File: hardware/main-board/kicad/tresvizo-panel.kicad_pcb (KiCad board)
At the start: 4 copper layers, 82.8 x 78 mm, 141 parts, among them J101 PANEL_USB, J102 BATTERY, J301 GNSS, J401 TF-015, J402 BOTON, J403 OLED, J404 NTC, J405 IMU, J406 LEDS, J501 USB_C, J502 PANEL_USB, Q101 AO3400A, Q102 AO3401A, Q103 AO3400A, Q401 AO3401A, Q402 AO3400A, SW201 RESET, SW202 BOOT, U101 USBLC6-2SC6, U102 BQ25798RQMR, U103 MAX17048G+T10, U105 TPS62903RPJR, U201 ESP32-S3-MINI-1-N4R2, U301 TPS63070RNMR, U302 USBLC6-2SC6, U303 USBLC6-2SC6, U501 USBLC6-2SC6

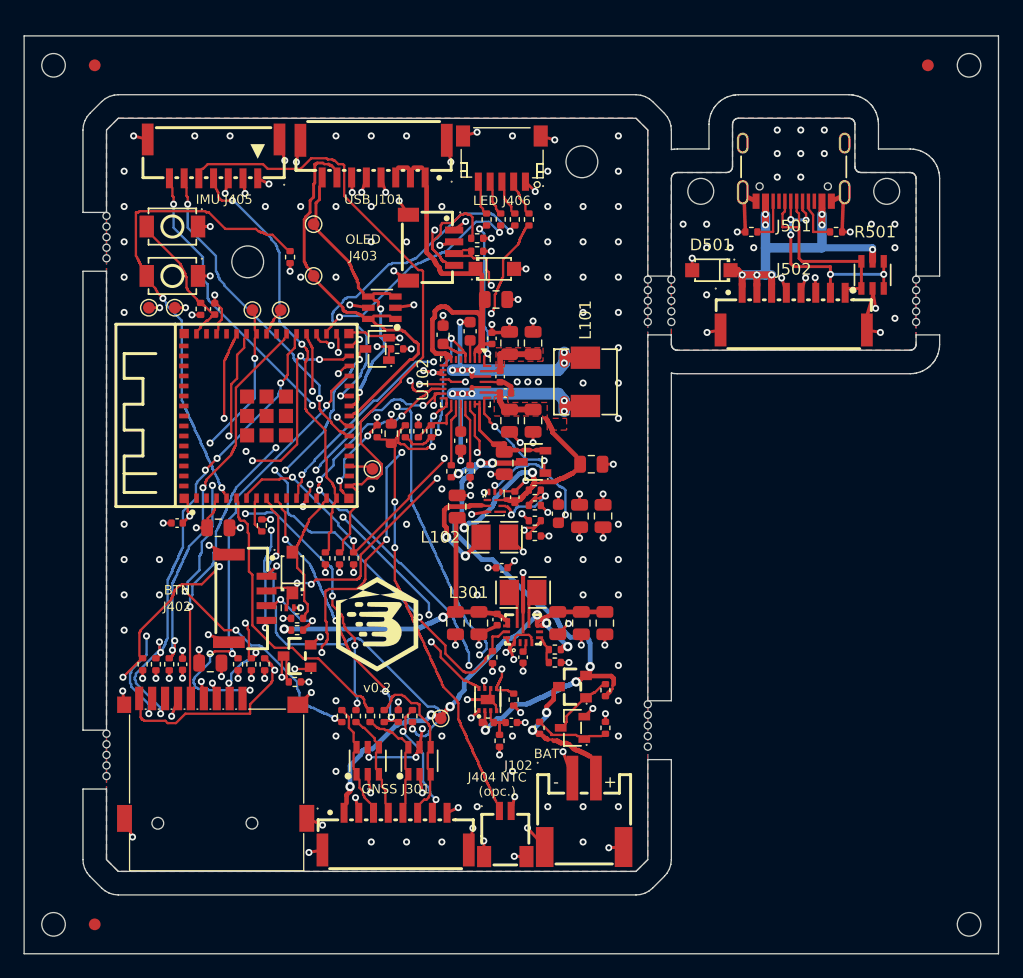
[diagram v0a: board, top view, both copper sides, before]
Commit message: Placa principal v0.2: J404 montado con puente JP101, USB-C de la panel-usb más volado, correcciones de la auditoría y logotipo
- J404 (NTC) se monta de fábrica y la NTC queda opcional. Sin ella, R106 (10 kΩ) va a GND por
  JP101, un puente de soldadura cerrado de fábrica, y el cargador ve 25 °C. Para usar la NTC se
  corta JP101 («cortar JP101» en la serigrafía, sobre el puente). R115 baja junto a R113 para
  dejar sitio a esa línea.
- panel-usb: el canto de la lengüeta retrocede 0.8 mm (v = 0.89) y el USB-C sobresale 1.29 mm; su
  cara sigue a ras de la tapa. El cobre queda a 0.41 mm del canto. En el panel la fresa frente al
  USB-C se ensancha a 3 mm (opción cuts de panelize.py) para dejar 1.71 mm hasta el marco; el
  panel pasa a 82.8 x 79 mm.
- Auditoría: VBUS de J101 al cargador con pistas de 0.8 y 1.0 mm, etiquetas de la batería y del
  NTC separadas, planos internos con 0.12 mm de margen y, en el README, medir el pin 1 de la
  carrier antes de enchufar el arnés y la ranura propuesta en la base bajo J102.
- Logotipo: las piezas con huecos se parten en tiras, porque KiCad deformaba al guardar los
  contornos fracturados (el distintivo de la cara de componentes salía mal).
- ERC 0; DRC con 0 errores, 0 avisos, 0 sin conectar y 0 diferencias de paridad en las dos placas
  y el panel. Comprobación en FreeCAD contra V2.2 sin choques nuevos. Costo estimado de montaje y
  piezas: 213.60 USD por 5 juegos en un panel (J404 suma 2.22 USD), sin el PCB desnudo.
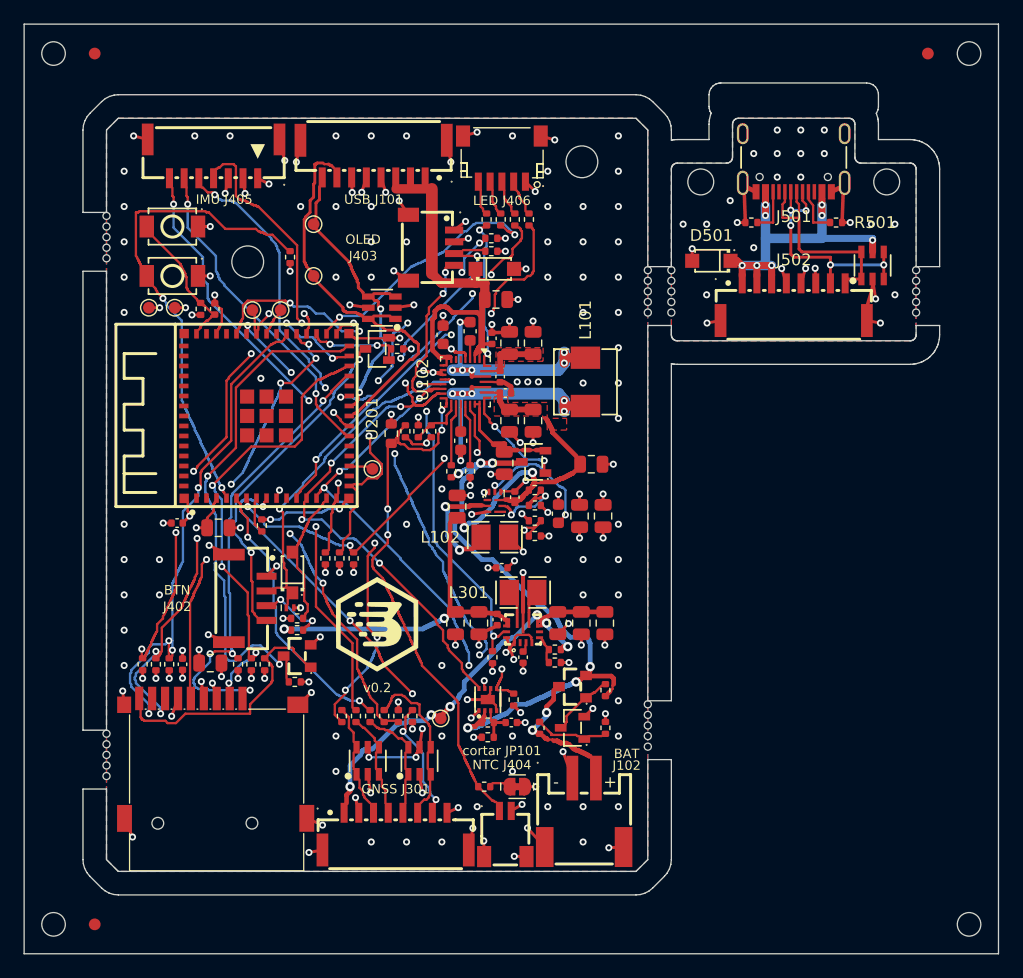
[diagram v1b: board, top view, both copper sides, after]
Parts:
- added JP101: NTC_CORTAR, tresvizo_lcsc:SolderJumper-2_P1.3mm_Bridged_RoundedPad1.0x1.5mm, F.Cu at (141.9, 163.8)
- moved R106 31.5 mm to (139.1, 163.8), turned to 0 degrees
- moved R204 1.20 mm to (139.7, 118.3)
- moved R205 1.20 mm to (139.7, 117.2)
- moved R115 1.04 mm to (139.4, 159.6), turned to 0 degrees
- moved FID1 1.00 mm to (106.0, 101.5)
- moved FID2 1.00 mm to (176.8, 101.5)
- moved TH1 1.00 mm to (102.5, 101.5)
- moved TH2 1.00 mm to (180.3, 101.5)
- moved U501 0.80 mm to (172.1, 119.5)
- moved D501 0.80 mm to (158.4, 119.1)
- moved H501 0.80 mm to (157.5, 112.4)
- moved H502 0.80 mm to (173.3, 112.4)
- moved J501 0.80 mm to (165.4, 110.8)
- moved J502 0.80 mm to (165.4, 122.6)
- moved MB3 0.80 mm to (153.0, 119.9)
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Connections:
- R106 pad 2: GND -> /Alimentación, carga y batería/CHG_TS_FIJA
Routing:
- net IMU_SCL: track 53.8 -> 40.3 mm, vias 0 -> 3
- net I2C_SCL: track 67.7 -> 55.8 mm, vias 7 -> 9
- net LED_G: track 30.3 -> 23.5 mm, vias 2 -> 3
- net FG_ALRT_N: track 38.3 -> 45.0 mm, vias 4 -> 6
- net GNSS_RESET_MCU: track 33.7 -> 28.4 mm, vias 2 -> 4
- net SD_D3: track 33.7 -> 37.9 mm
- net I2C_SDA: track 64.5 -> 60.4 mm, vias 9 -> 7
- net SD_CLK: track 34.2 -> 37.7 mm, vias 3 -> 2
- net GNSS_PWR_EN: track 44.6 -> 47.9 mm, vias 3 -> 4
- net /Alimentación, carga y batería/VBUS: track 34.0 -> 37.3 mm
- net IMU_SDA: track 35.3 -> 38.2 mm
- net ESP_TX0: track 44.1 -> 46.9 mm, vias 6 -> 4
- net /Alimentación, carga y batería/VPACK: track 50.6 -> 53.3 mm
- net LED_B: track 19.3 -> 21.3 mm
- net BTN_N: track 30.7 -> 28.8 mm, vias 4 -> 2
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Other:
- board size 82.8 x 78 mm -> 82.8 x 79 mm
- board text added: "NTC J404"
- board text added: "cortar JP101"
- board text removed: "(opc.)"
- board text removed: "J404 NTC"

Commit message: Placa principal v0.2: techo de entrada del USB a ~1.45 A (R102 22k -> 8.2k)
Revisión del propietario: con ILIM en 10k/22k el cargador podía pedir ~2.9 A a cualquier puerto,
sin detectar cuánto da. Con 10k/8.2k desde REGN (4.6-5.0 V) el techo queda en 1.34-1.56 A, que
alcanza para cargar 1S a 1 A con el equipo encendido. La variante 2S vuelve a 22k (~2.9 A).
Solo cambia el valor de R102 (C25924): pistas y gerbers de cobre iguales; ERC 0, DRC 0 en la
placa y en el panel, paridad 0.

README: queda para v0.3 la detección por CC del USB-C y el par diferencial D+/D-, que pide
invertir los pines 7/8 de J101 y J502. En Full Speed la diferencia de largo actual (9 mm, unos
60 ps) no afecta.
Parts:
- R102: value 22k -> 8.2k

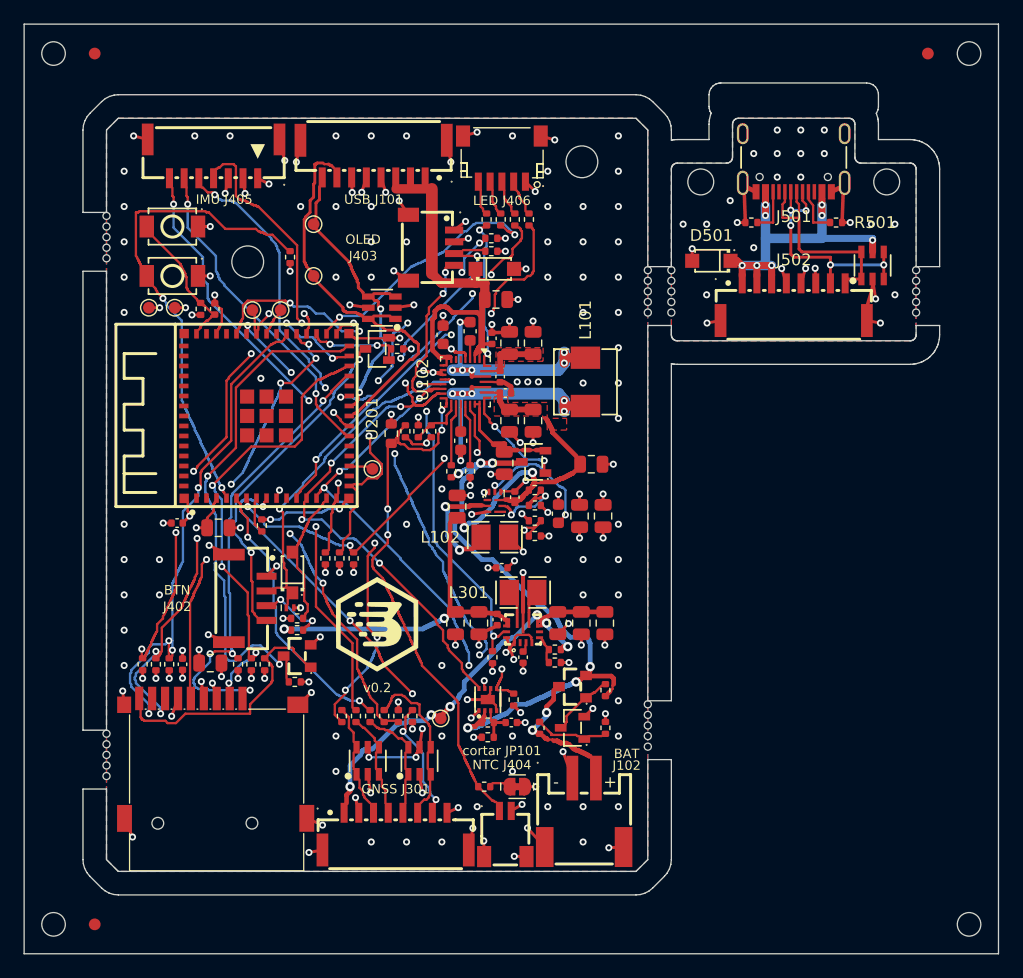
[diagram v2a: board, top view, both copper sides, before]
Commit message: Placa principal v0.2: ESP32-S3-WROOM-1-N16R2 en lugar del MINI-1 y sin LEDs del panel
- U201 = ESP32-S3-WROOM-1-N16R2 (C2913205): 16 MB de flash y 2 MB de PSRAM quad. Huella y
  modelos de LCSC; el .step se corrió 3.65 mm para que coincida con su .wrl y la huella.
- GPIO nuevos para rutear el módulo en la misma placa: microSD CLK 6, CMD 7, D0 5, D1 4, D2 16,
  D3 15 y detección 17; UART del GNSS TX 8 / RX 9; PPS 10, EVENT 11, RESET 12; I2C 13/14;
  IMU 41/42 con INT1 2 e INT3 1; botón 18; puntos de prueba en 35, 36 y 37. README y pinout
  con el mapa para el firmware.
- Fuera J406, sus resistencias y la del STAT del cargador: la carcasa V2.3 no lleva LEDs.
- Misma placa de 46 x 64 mm. H1 pasa a (12.0, 9.6) y el corte del riel +X frente a la antena a
  v 15.1-34.0; antena sin cobre en u 0-6.7, v 15.7-33.7.
- R108 sale de debajo de los pines de la microSD (el ruteador se ciclaba entre SD_D3 y
  CHG_INT_N) y el divisor de TS va bajo L102.
- BUCK_SW y el PGND de U105 prerruteados: la vía que el ruteador ponía junto a L102 hacía caer
  el relleno de zonas de KiCad 10 (-11, también en kicad-cli). route_rest guarda las pistas que
  arranca mientras dura el ruteo.
- DRC 0, sin conexiones pendientes y con paridad en la placa y en el panel; ERC 0. Costo
  estimado 206.86 USD por 5 juegos (montaje + piezas, sin PCB).
- Carcasa V2.3: H1 en z 77.9, riel +X cortado en z 53.7-72.4, placa superior recortada frente
  a la antena y SMA de la carrier con las medidas de la foto. Placa nueva contra la carcasa:
  0 mm3 de choques.
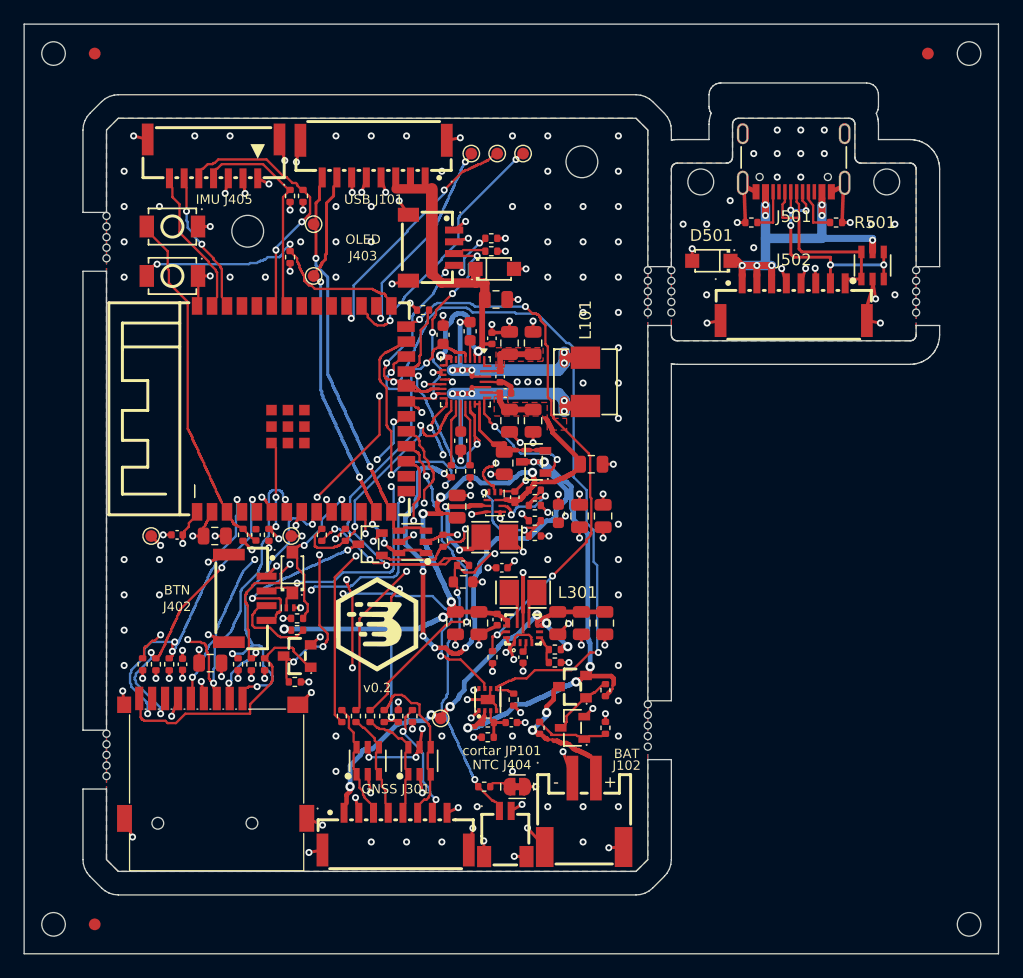
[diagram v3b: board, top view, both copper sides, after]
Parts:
- removed J406: LEDS, tresvizo_lcsc:CONN-SMD_SM05B-SRSS-TB-LF-SN
- removed R119: 22k, Resistor_SMD:R_0402_1005Metric
- removed R413: 100k, Resistor_SMD:R_0402_1005Metric
- removed R414, R415: 4.7k, Resistor_SMD:R_0402_1005Metric
- R109: value 1k -> 1M
- R110: value 1M -> 100k
- R111: value 100k -> 1M
- R112: value 1M -> 0
- R113: value 0 -> 10k
- R114: value 10k -> 0
- R115: value 0 -> 22k
- R116: value 22k -> 10k
- R117: value 10k -> 100k
- R118: value 100k -> 22k
- R409: value 1k -> 100
- R410: value 100 -> 100k
- R411, R412: value 100 -> 4.7k
- TP203: value IO14 -> IO35
- TP204: value IO42 -> IO36
- TP205: value TXD0 -> IO37
- U201: value ESP32-S3-MINI-1-N4R2 -> ESP32-S3-WROOM-1-N16R2; footprint tresvizo_lcsc:BULETM-SMD_ESP32-S3-MINI-1-N8 -> tresvizo_lcsc:WIRELM-SMD_ESP32-S3-WROOM-1
- moved R109 41.3 mm to (149.4, 155.6)
- moved R409 40.1 mm to (123.2, 150.5), turned to 0 degrees
- moved R412 36.9 mm to (123.7, 113.6), turned to 90 degrees
- moved TP203 28.1 mm to (138.0, 110.0)
- moved R410 28.0 mm to (135.6, 142.9)
- moved TP205 24.7 mm to (140.2, 110.0)
- moved TP204 24.5 mm to (142.4, 110.0)
- moved R108 21.9 mm to (133.9, 123.3), turned to 0 degrees
- moved TP202 21.8 mm to (122.7, 142.5)
- moved R115 21.4 mm to (143.4, 138.6)
- moved U101 20.1 mm to (133.0, 143.0)
- moved R201 19.5 mm to (118.6, 142.4)
- moved C203 19.5 mm to (119.7, 142.4)
- moved TP201 19.4 mm to (110.8, 142.5)
- moved R411 18.0 mm to (122.6, 113.6)
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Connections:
- R109 pad 1: /Alimentación, carga y batería/CHG_STAT -> /Alimentación, carga y batería/VPACK
- R109 pad 2: CHG_LED_K -> /Alimentación, carga y batería/BATREV_G
- R110 pad 1: /Alimentación, carga y batería/VPACK -> /Alimentación, carga y batería/VBATT_IN
- R110 pad 2: /Alimentación, carga y batería/BATREV_G -> /Alimentación, carga y batería/BATREV_SENSE
- R111 pad 1: /Alimentación, carga y batería/VBATT_IN -> /Alimentación, carga y batería/BATREV_SENSE
- R111 pad 2: /Alimentación, carga y batería/BATREV_SENSE -> GND
- R112 pad 1: /Alimentación, carga y batería/BATREV_SENSE -> /Alimentación, carga y batería/VPACK
- R112 pad 2: GND -> /Alimentación, carga y batería/FG_VDD
- R113 pad 1: /Alimentación, carga y batería/VPACK -> +3V3
- R113 pad 2: /Alimentación, carga y batería/FG_VDD -> FG_ALRT_N
- R114 pad 2: FG_ALRT_N -> /Alimentación, carga y batería/FG_VDD
- R115 pad 1: +3V3 -> VSYS
- R115 pad 2: /Alimentación, carga y batería/FG_VDD -> /Alimentación, carga y batería/BUCK_EN
- R116 pad 1: VSYS -> /Alimentación, carga y batería/BUCK_EN
- R116 pad 2: /Alimentación, carga y batería/BUCK_EN -> GND
- R117 pad 1: /Alimentación, carga y batería/BUCK_EN -> +3V3
- R117 pad 2: GND -> /Alimentación, carga y batería/BUCK_FB
- R118 pad 1: +3V3 -> /Alimentación, carga y batería/BUCK_FB
- R118 pad 2: /Alimentación, carga y batería/BUCK_FB -> GND
- R304 pad 1: ESP_TX0 -> GNSS_TX_MCU
- R409 pad 1: LED_R -> VSYS
- R409 pad 2: /microSD, IMU por conector y panel/LED_R_K -> /microSD, IMU por conector y panel/BTN_LED_A
- R410 pad 1: LED_G -> BTN_LED_EN
- R410 pad 2: /microSD, IMU por conector y panel/LED_G_K -> GND
- R411 pad 1: LED_B -> +3V3
- R411 pad 2: /microSD, IMU por conector y panel/LED_B_K -> IMU_SDA
- R412 pad 1: VSYS -> +3V3
- R412 pad 2: /microSD, IMU por conector y panel/BTN_LED_A -> IMU_SCL
- TP203 pad 1: /ESP32-S3/ESP_IO14 -> /ESP32-S3/ESP_IO35
- TP204 pad 1: /ESP32-S3/ESP_IO42 -> /ESP32-S3/ESP_IO36
- TP205 pad 1: ESP_TX0 -> /ESP32-S3/ESP_IO37
- U102 pad 1: /Alimentación, carga y batería/CHG_STAT -> unconnected-(U102-STAT-Pad1)
- U201 pad 10: unconnected-(U201-IO6-Pad10) -> SD_DET
- U201 pad 11: LED_R -> BTN_SENSE_N
- U201 pad 12: I2C_SDA -> GNSS_TX_MCU
- U201 pad 13: I2C_SCL -> USB_DN
- U201 pad 14: BTN_SENSE_N -> USB_DP
- U201 pad 15: IMU_SDA -> /ESP32-S3/ESP_IO3
- U201 pad 16: IMU_SCL -> unconnected-(U201-IO46-Pad16)
- U201 pad 17: unconnected-(U201-IO13-Pad17) -> GNSS_TXD2_MCU
- U201 pad 18: /ESP32-S3/ESP_IO14 -> GNSS_PPS_MCU
- U201 pad 19: unconnected-(U201-IO15-Pad19) -> GNSS_EVENT_MCU
- U201 pad 2: GND -> +3V3
- U201 pad 20: unconnected-(U201-IO16-Pad20) -> GNSS_RESET_MCU
- U201 pad 21: IMU_INT1 -> I2C_SDA
- U201 pad 22: IMU_INT3 -> I2C_SCL
- U201 pad 23: USB_DN -> CHG_INT_N
- U201 pad 24: USB_DP -> FG_ALRT_N
- U201 pad 25: LED_G -> BTN_LED_EN
- U201 pad 26: unconnected-(U201-IO26-Pad26) -> GNSS_PWR_EN
- U201 pad 27: SD_D2 -> /ESP32-S3/ESP_BOOT
- U201 pad 28: SD_D3 -> /ESP32-S3/ESP_IO35
- U201 pad 29: SD_CMD -> /ESP32-S3/ESP_IO36
- U201 pad 3: +3V3 -> /ESP32-S3/ESP_EN
- U201 pad 30: SD_DET -> /ESP32-S3/ESP_IO37
- U201 pad 31: FG_ALRT_N -> unconnected-(U201-IO38-Pad31)
- U201 pad 32: LED_B -> unconnected-(U201-IO39-Pad32)
- U201 pad 33: BTN_LED_EN -> unconnected-(U201-IO40-Pad33)
- U201 pad 34: SD_CLK -> IMU_SDA
- U201 pad 35: SD_D0 -> IMU_SCL
- U201 pad 36: SD_D1 -> unconnected-(U201-RXD0-Pad36)
- U201 pad 38: /ESP32-S3/ESP_IO42 -> IMU_INT1
- U201 pad 39: ESP_TX0 -> IMU_INT3
- U201 pad 4: /ESP32-S3/ESP_BOOT -> SD_D1
- U201 pad 40: GNSS_TXD2_MCU -> GND
- U201 pad 41: GNSS_PWR_EN -> GND
- U201 pad 5: GNSS_PPS_MCU -> SD_D0
- U201 pad 6: CHG_INT_N -> SD_CLK
- U201 pad 7: /ESP32-S3/ESP_IO3 -> SD_CMD
- U201 pad 8: GNSS_RESET_MCU -> SD_D3
- U201 pad 9: GNSS_EVENT_MCU -> SD_D2
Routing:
- net ESP_TX0: track 46.9 -> 0.00 mm, vias 4 -> 0
- net /Alimentación, carga y batería/REGN: track 15.4 -> 49.6 mm, vias 2 -> 4
- net LED_R: track 33.7 -> 0.00 mm, vias 3 -> 0
- net /Alimentación, carga y batería/VPACK: track 53.3 -> 86.6 mm, vias 6 -> 10
- net BTN_LED_EN: track 7.38 -> 33.8 mm, vias 2 -> 3
- net SD_DET: track 43.9 -> 19.0 mm, vias 2 -> 4
- net LED_G: track 23.5 -> 0.00 mm, vias 3 -> 0
- net IMU_SDA: track 38.2 -> 16.1 mm, vias 2 -> 0
- net LED_B: track 21.3 -> 0.00 mm, vias 2 -> 0
- net /ESP32-S3/ESP_IO36: track 0.00 -> 21.2 mm, vias 0 -> 2
- net IMU_SCL: track 40.3 -> 20.0 mm, vias 3 -> 2
- net /ESP32-S3/ESP_IO37: track 0.00 -> 19.9 mm, vias 0 -> 2
- net /ESP32-S3/ESP_IO3: track 2.47 -> 21.2 mm, vias 0 -> 3
- net GNSS_TX_MCU: track 0.00 -> 18.2 mm, vias 0 -> 2
- net SD_D0: track 42.5 -> 24.2 mm, vias 7 -> 4
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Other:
- board text added: "1S: R103=4.7k R116=10k U103=MAX17048"
- board text added: "2S: R103=8.2k R116=3.9k U103=MAX17049 R112 NC R114 0R"
- board text removed: "1S: R103=4.7k R117=10k U103=MAX17048"
- board text removed: "2S: R103=8.2k R117=3.9k U103=MAX17049 R113 NC R115 0R"
- board text removed: "LED J406"

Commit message: Placa principal v0.2: build reproducible, J301 en SH 8 y montaje en V2.3 con la carrier real
- Build reproducible: kiid_seed.py siembra los KIID de KiCad en cada paso con el contenido de sus
  entradas (sin las líneas de fecha y ruta de la netlist), y route_rest.py toma del DRC solo qué dos
  islas unir y elige siempre los mismos extremos. Dos builds completos dieron los mismos PCB,
  esquemáticos, BOM, CPL, mapa de pines y Gerber; solo cambian las fechas.
- route_rest.py corta los ciclos de arranque (3 por par de conexiones, 20 por conexión en total),
  guarda lo ruteado antes del relleno de zonas y admite ROUTE_FIRST. build.py rutea primero el bus
  de la microSD: con el WROOM, si otras redes toman antes el paso entre el ESP32, J402 y el zócalo,
  SD_CLK y SD_D2 se quedan sin ruta.
- build.py: PYTHONUNBUFFERED, para que un paso que se cae deje sus últimas líneas, y el error dice
  el script y la señal.
- J301 pasa de GH 8 a SH 8 (SM08B-SRSS-TB, C160407; huella de LCSC con anclajes MP y su modelo):
  ya no se puede cruzar con J101, que es GH 8 y lleva VBUS. Va en v 60.7, con la boca en el canto.
  Suma 2.25 USD a los 5 juegos: 209.11 USD.
- Gerber, vistas y esquema en PDF fuera de git salvo en los hitos (.gitignore y nota en los README).
  El quitado del índice quedó por error en b94647d.
- cad/: STEP regenerados con esta placa (modelos de LCSC corregidos por su .wrl) y placement.json al
  día. Nuevo carrier_bdlx.py: la carrier aproximada con sus componentes, sacada de la foto.
  check_montaje_v2_3.py:
  - mueve la placa desplazamiento_placa_y;
  - prueba también la carrier con componentes: encontró los choques de su USB-C y de las soldaduras
    del arnés, que b94647d corrige;
  - lleva el cable de la 18650 1 mm más adelante junto al riel -X.
- ERC 0. DRC con 0 violaciones, 0 sin conectar y 0 de paridad en la placa, la panel-usb y el panel;
  133 de 133 conexiones. Montaje en V2.3 (b94647d) sin choques paso a paso; el cable de la 18650
  pasa libre, a 0.17 mm como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
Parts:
- J301: footprint tresvizo_lcsc:CONN-SMD_8P-P1.25_XUNPU-WAFER-GH1.25-8PWB -> tresvizo_lcsc:CONN-TH_SM08B-SRSS-TB-LF-SN
- moved J301 0.10 mm to (131.6, 167.7)
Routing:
- net /Alimentación, carga y batería/VPACK: track 86.6 -> 48.0 mm, vias 10 -> 6
- net BTN_LED_EN: track 33.8 -> 65.4 mm, vias 3 -> 5
- net FG_ALRT_N: track 62.6 -> 33.8 mm, vias 2 -> 3
- net VSYS: track 65.6 -> 91.1 mm, vias 6 -> 8
- net GNSS_PWR_EN: track 46.8 -> 33.7 mm
- net I2C_SCL: track 69.5 -> 77.8 mm, vias 9 -> 7
- net SD_D3: track 19.7 -> 27.9 mm
- net BTN_N: track 29.6 -> 37.5 mm, vias 3 -> 6
- net /ESP32-S3/ESP_IO3: track 21.2 -> 13.5 mm, vias 3 -> 2
- net USB_DP: track 31.4 -> 38.0 mm, vias 2 -> 5
- net GNSS_PPS_MCU: track 29.0 -> 23.7 mm
- net /GNSS: carrier UM980 por conector y su 5 V/GNSS_EVENT: track 11.3 -> 16.2 mm
- net CHG_TS: track 42.6 -> 38.0 mm, vias 5 -> 4
- net SD_DET: track 19.0 -> 14.7 mm, vias 4 -> 2
- net /GNSS: carrier UM980 por conector y su 5 V/GNSS_RXD2: track 6.60 -> 10.8 mm
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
